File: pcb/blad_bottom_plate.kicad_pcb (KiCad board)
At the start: 2 copper layers, 228.6 x 76.2 mm, 6 parts

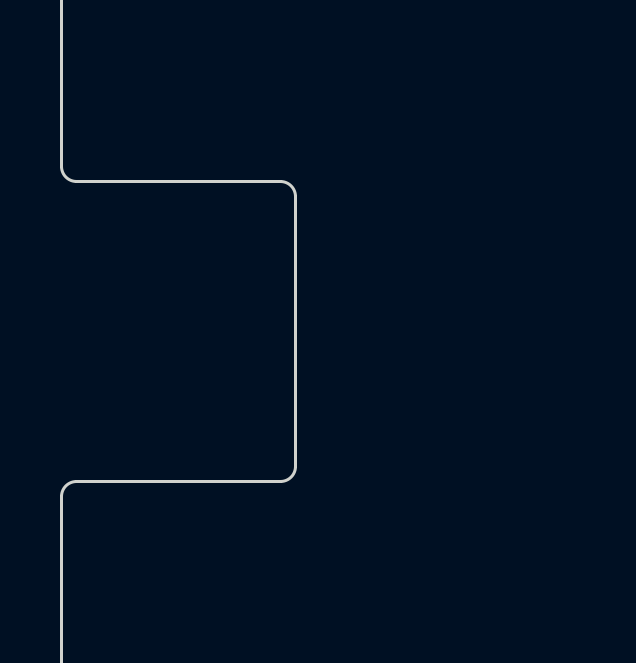
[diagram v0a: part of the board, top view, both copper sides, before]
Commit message: Add mounting holes and update case geometry
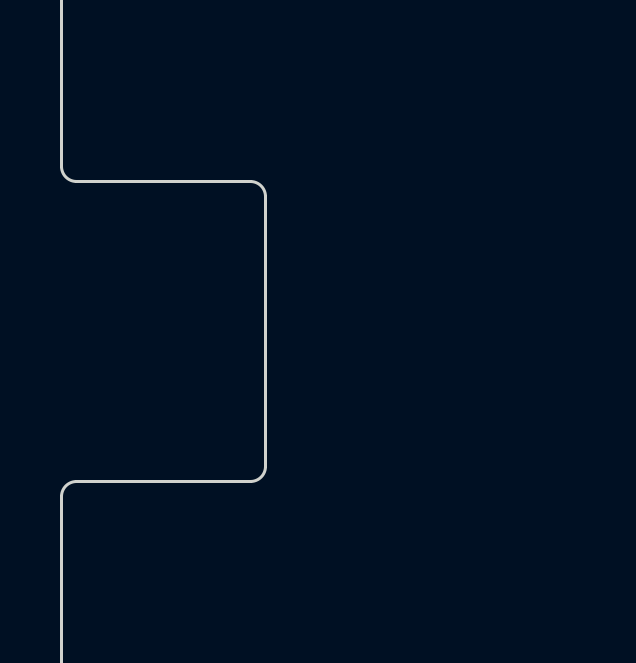
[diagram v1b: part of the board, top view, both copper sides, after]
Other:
- outline, holes or cut-outs redrawn
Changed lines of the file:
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@@
 		(filling no)
 		(pcbplotparams
-			(layerselection 0x00000000_00000000_55555555_5755f5ff)
+			(layerselection 0x00000000_00000000_55555555_555555d0)
 			(plot_on_all_layers_selection 0x00000000_00000000_00000000_00000000)
 			(disableapertmacros no)
@@
 			(pdf_single_document no)
 			(dxfpolygonmode yes)
-			(dxfimperialunits yes)
+			(dxfimperialunits no)
 			(dxfusepcbnewfont yes)
 			(psnegative no)
@@
 			(crossoutdnponfab yes)
 			(subtractmaskfromsilk no)
-			(outputformat 1)
+			(outputformat 3)
 			(mirror no)
-			(drillshape 1)
+			(drillshape 0)
 			(scaleselection 1)
-			(outputdirectory "")
+			(outputdirectory "../case/")
 		)
 	)
@@
 	(gr_line
 		(start 90.19375 146.606249)
-		(end 96.99375 146.60625)
+		(end 95.99375 146.60625)
 		(stroke
 			(width 0.1)
@@
 	)
 	(gr_arc
-		(start 96.99375 146.60625)
-		(mid 97.347302 146.752697)
-		(end 97.49375 147.106249)
+		(start 95.99375 146.60625)
+		(mid 96.347302 146.752697)
+		(end 96.49375 147.10625)
 		(stroke
 			(width 0.1)
@@
 	)
 	(gr_line
-		(start 96.993748 156.606249)
+		(start 95.993751 156.606249)
 		(end 90.19375 156.606249)
 		(stroke
@@
 	)
 	(gr_line
-		(start 97.49375 147.106249)
-		(end 97.49375 156.106249)
+		(start 96.49375 147.10625)
+		(end 96.49375 156.10625)
 		(stroke
 			(width 0.1)
@@
 	)
 	(gr_arc
-		(start 97.49375 156.106249)
-		(mid 97.347302 156.459803)
-		(end 96.993748 156.606249)
+		(start 96.49375 156.10625)
+		(mid 96.347303 156.459802)
+		(end 95.993751 156.606249)
 		(stroke
 			(width 0.1)
@@
 	)
 	(group ""
-		(members "17145901-475b-4616-82e1-dcc0b701e4bf" "1fd71d70-de9d-4894-bf33-25f6edd597d2"
-			"211e9d9b-86ef-475f-a827-852d0eb563f7" "2271729f-9ee0-4d69-a004-4a47236f839f"
-			"315d96c1-1881-462d-a7c0-51b5e5125f40" "379dde88-a257-4529-82c2-8d0351c74444"
-			"40666318-c9cd-41b7-8a53-1529c4a9d253" "40c4fe29-fc29-433e-ace2-4d8ef901fdfc"
-			"421bbcb7-ddf2-48be-8344-8eb7c7a51f55" "4e8b78b7-c20b-4928-9b83-e7cb29da93f6"
-			"63f703fd-95ff-4286-b1ce-b326aa7237cc" "7cefd275-e157-4536-a9f7-fbb3d93f402b"
-			"7dcc4da9-ddb4-4e3b-8523-2aeac3b939cd" "81ad9bd4-2c01-45ca-a457-450304155fdc"
-			"89b01bf5-ef15-4867-bd50-50d34fc3914f" "8f540864-37ee-4f37-bc42-3dff816e9df1"
-			"c8dbc5b5-cda7-493a-b886-ba6e941ec231" "d0f308d8-d5e3-42ce-b68b-6f69628c9db5"
-			"d7228916-0474-4942-b449-a27a7cbb7957" "d7296631-fa01-4f07-a2c4-f843e7b1f084"
-			"f26520b3-8c45-4f12-95df-143b0639d80b" "f44c0cea-6b07-44b4-93d2-f0ae9c38df59"
-		)
-	)
+		(members "0472c3b5-6bf8-4187-a4ce-cb52493cf091" "06d008e3-ea8b-4315-bc74-d809ca88ec49"
+			"0b854390-58ca-44f9-9a75-085cd222cc4c" "0beeae07-1a83-49cf-8255-262c77e9af92"
+			"10c98cbe-8647-431a-956f-24ecf69f26db" "10ca2a12-6528-4cb7-9720-3744ad96b8e6"
+			"150b5458-0fdb-44ba-ae9c-624d5b2dc097" "292bc2c7-c8ad-4efd-997e-c774e5ae5a4c"
+			"421859e0-c852-4a81-8d2f-dcdbcf6c8653" "7d7948e9-e0c6-423b-adbb-c8dae435b648"
+			"7ddaab6a-47fb-4109-848c-407eba71045c" "a2d865a0-f5c9-4fc8-aff4-9c98de92b1db"
+			"a4f8a2af-3472-4778-962a-ceb1da0de908" "a53b3724-e0bc-48a3-9629-653f3bd96111"
+			"ac23b05d-2e9e-46ff-97e1-e26c859fd1e4" "af5a773c-27d1-4d66-a41b-62e35a14cd8b"
+			"b206beb2-540c-4e41-9a53-bd92d6d099fb" "b78edd60-c10a-4ef6-8962-5f049a71c6a8"
+			"bea16699-3f97-4309-ad03-92fec9a88be3" "bff7b4a8-1430-4023-ad1c-1f8a440674f7"
+			"ce8211af-59c9-49fa-8603-800c2b3247ad" "da90de73-0f30-4204-a148-d2ccc74b86db"
+		)
+	)

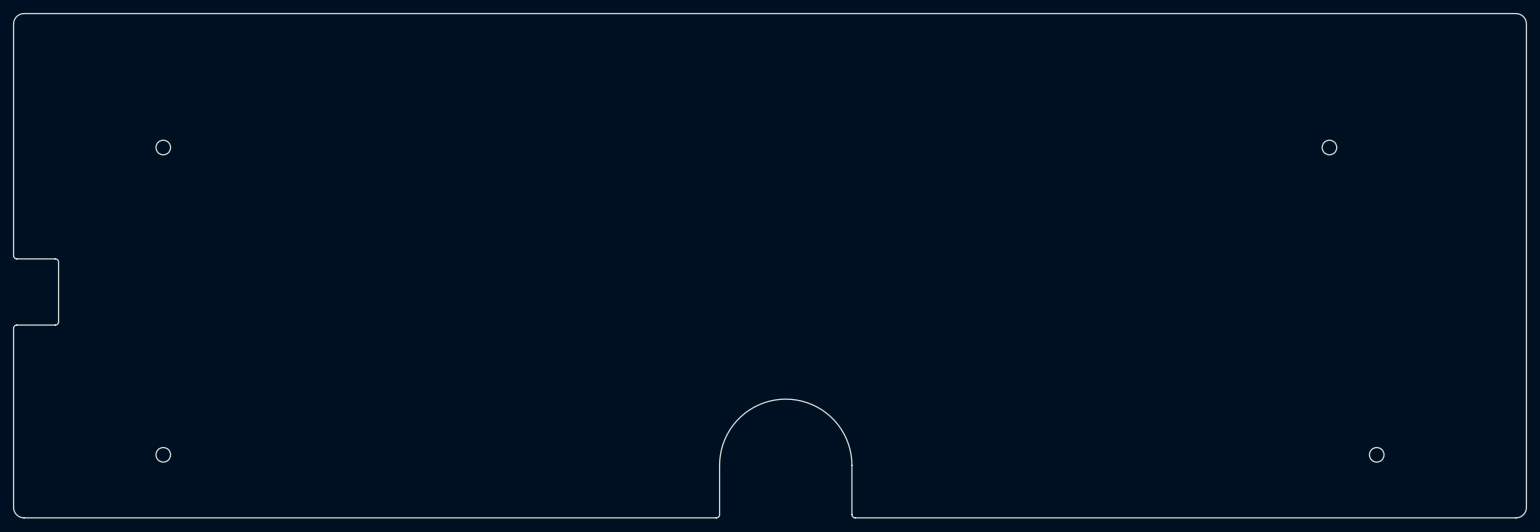
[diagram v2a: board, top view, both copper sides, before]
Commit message: Update hardware design and bottom view render
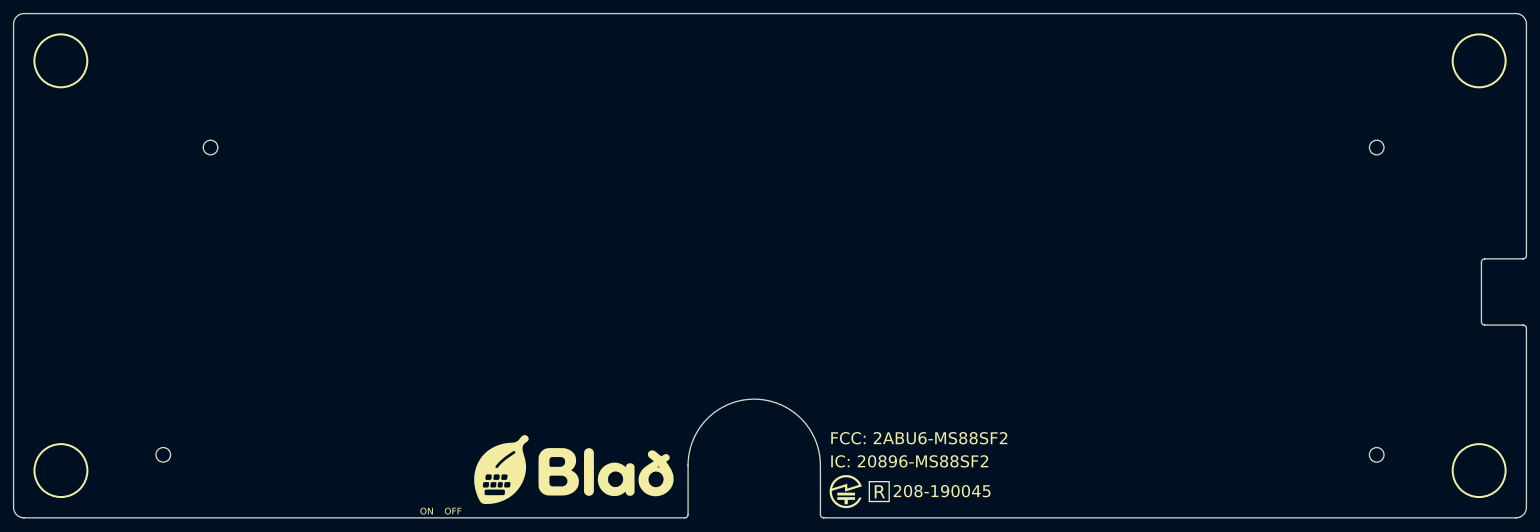
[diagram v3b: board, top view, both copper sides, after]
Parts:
- removed the G*** at (192.5, 175.8)
- added G***: LOGO, Smidr:TechMark_MS88SF21, F.Cu at (215.5, 181.8)
- G***: moved to F.Cu
- REF** (x4): moved to B.Cu
- moved REF** 183.4 mm to (295.7, 129.8), turned to 180 degrees
- moved REF** 183.4 mm to (112.3, 176.2), turned to 180 degrees
- moved REF** 183.4 mm to (295.7, 176.2), turned to 180 degrees
- moved REF** 169.1 mm to (119.5, 129.8), turned to 180 degrees
- moved G*** 59.1 mm to (174.4, 178.8), turned to 0 degrees
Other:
- outline, holes or cut-outs redrawn
- board text added: "OFF"
- board text added: "ON"

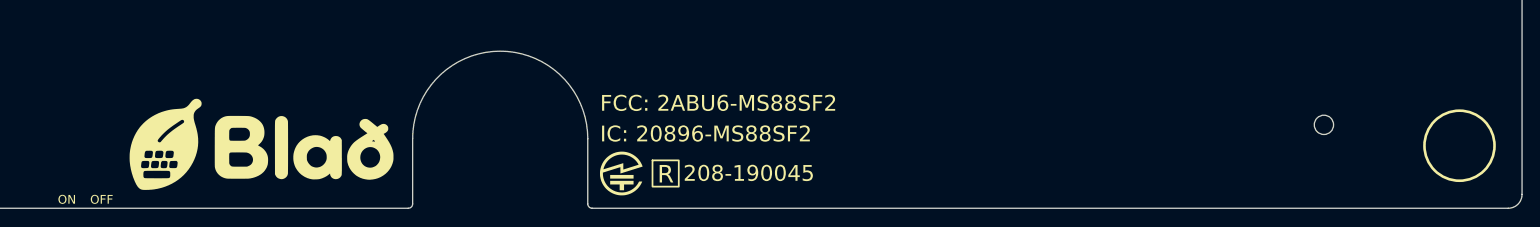
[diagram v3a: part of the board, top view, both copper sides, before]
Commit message: Update keyboard design and renderings
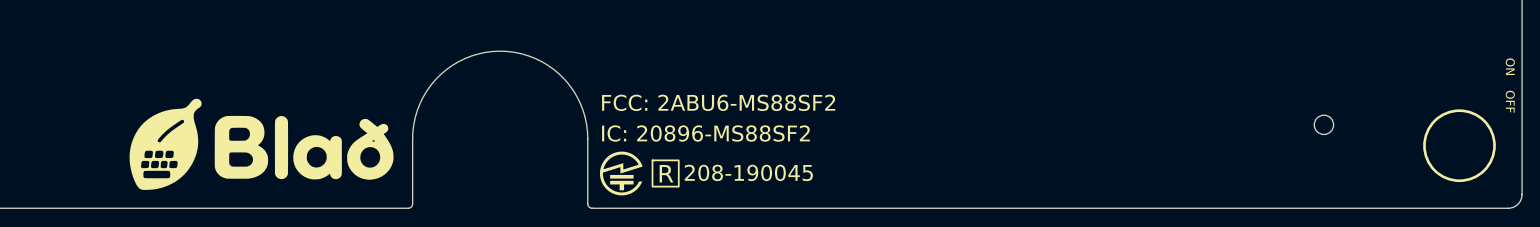
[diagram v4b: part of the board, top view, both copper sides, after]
